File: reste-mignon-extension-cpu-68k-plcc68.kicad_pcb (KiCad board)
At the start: 4 copper layers, 99.1 x 99.1 mm, 20 parts, among them J1 RESTE_MIGNON_CPU_CONNECTOR_A, J2 RESTE_MIGNON_CPU_CONNECTOR_B, U1 MC68000_PLCC_68_PHY

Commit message: switch RN5 and RN6 to ease routing
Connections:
- RN5 pad 2: /D0 -> /D8
- RN5 pad 3: /D1 -> /D9
- RN5 pad 4: /D2 -> /D10
- RN5 pad 5: /D3 -> /D11
- RN5 pad 6: /D4 -> /D12
- RN5 pad 7: /D5 -> /D13
- RN5 pad 8: /D6 -> /D14
- RN5 pad 9: /D7 -> /D15
- RN6 pad 2: /D8 -> /D0
- RN6 pad 3: /D9 -> /D1
- RN6 pad 4: /D10 -> /D2
- RN6 pad 5: /D11 -> /D3
- RN6 pad 6: /D12 -> /D4
- RN6 pad 7: /D13 -> /D5
- RN6 pad 8: /D14 -> /D6
- RN6 pad 9: /D15 -> /D7
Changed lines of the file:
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@@
       (net 1 "/VCC") (pinfunction "common") (pintype "passive"))
     (pad "2" thru_hole oval (at 2.54 0 90) (size 1.6 1.6) (drill 0.8) (layers "*.Cu" "*.Mask")
-      (net 42 "/D0") (pinfunction "R1") (pintype "passive"))
+      (net 50 "/D8") (pinfunction "R1") (pintype "passive"))
     (pad "3" thru_hole oval (at 5.08 0 90) (size 1.6 1.6) (drill 0.8) (layers "*.Cu" "*.Mask")
-      (net 41 "/D1") (pinfunction "R2") (pintype "passive"))
+      (net 49 "/D9") (pinfunction "R2") (pintype "passive"))
     (pad "4" thru_hole oval (at 7.62 0 90) (size 1.6 1.6) (drill 0.8) (layers "*.Cu" "*.Mask")
-      (net 43 "/D2") (pinfunction "R3") (pintype "passive"))
+      (net 52 "/D10") (pinfunction "R3") (pintype "passive"))
     (pad "5" thru_hole oval (at 10.16 0 90) (size 1.6 1.6) (drill 0.8) (layers "*.Cu" "*.Mask")
-      (net 45 "/D3") (pinfunction "R4") (pintype "passive"))
+      (net 51 "/D11") (pinfunction "R4") (pintype "passive"))
     (pad "6" thru_hole oval (at 12.7 0 90) (size 1.6 1.6) (drill 0.8) (layers "*.Cu" "*.Mask")
-      (net 44 "/D4") (pinfunction "R5") (pintype "passive"))
+      (net 53 "/D12") (pinfunction "R5") (pintype "passive"))
     (pad "7" thru_hole oval (at 15.24 0 90) (size 1.6 1.6) (drill 0.8) (layers "*.Cu" "*.Mask")
-      (net 47 "/D5") (pinfunction "R6") (pintype "passive"))
+      (net 55 "/D13") (pinfunction "R6") (pintype "passive"))
     (pad "8" thru_hole oval (at 17.78 0 90) (size 1.6 1.6) (drill 0.8) (layers "*.Cu" "*.Mask")
-      (net 46 "/D6") (pinfunction "R7") (pintype "passive"))
+      (net 54 "/D14") (pinfunction "R7") (pintype "passive"))
     (pad "9" thru_hole oval (at 20.32 0 90) (size 1.6 1.6) (drill 0.8) (layers "*.Cu" "*.Mask")
-      (net 48 "/D7") (pinfunction "R8") (pintype "passive"))
+      (net 57 "/D15") (pinfunction "R8") (pintype "passive"))
     (model "${KICAD6_3DMODEL_DIR}/Resistor_THT.3dshapes/R_Array_SIP9.wrl"
       (offset (xyz 0 0 0))
@@
       (net 1 "/VCC") (pinfunction "common") (pintype "passive"))
     (pad "2" thru_hole oval (at 2.54 0 90) (size 1.6 1.6) (drill 0.8) (layers "*.Cu" "*.Mask")
-      (net 50 "/D8") (pinfunction "R1") (pintype "passive"))
+      (net 42 "/D0") (pinfunction "R1") (pintype "passive"))
     (pad "3" thru_hole oval (at 5.08 0 90) (size 1.6 1.6) (drill 0.8) (layers "*.Cu" "*.Mask")
-      (net 49 "/D9") (pinfunction "R2") (pintype "passive"))
+      (net 41 "/D1") (pinfunction "R2") (pintype "passive"))
     (pad "4" thru_hole oval (at 7.62 0 90) (size 1.6 1.6) (drill 0.8) (layers "*.Cu" "*.Mask")
-      (net 52 "/D10") (pinfunction "R3") (pintype "passive"))
+      (net 43 "/D2") (pinfunction "R3") (pintype "passive"))
     (pad "5" thru_hole oval (at 10.16 0 90) (size 1.6 1.6) (drill 0.8) (layers "*.Cu" "*.Mask")
-      (net 51 "/D11") (pinfunction "R4") (pintype "passive"))
+      (net 45 "/D3") (pinfunction "R4") (pintype "passive"))
     (pad "6" thru_hole oval (at 12.7 0 90) (size 1.6 1.6) (drill 0.8) (layers "*.Cu" "*.Mask")
-      (net 53 "/D12") (pinfunction "R5") (pintype "passive"))
+      (net 44 "/D4") (pinfunction "R5") (pintype "passive"))
     (pad "7" thru_hole oval (at 15.24 0 90) (size 1.6 1.6) (drill 0.8) (layers "*.Cu" "*.Mask")
-      (net 55 "/D13") (pinfunction "R6") (pintype "passive"))
+      (net 47 "/D5") (pinfunction "R6") (pintype "passive"))
     (pad "8" thru_hole oval (at 17.78 0 90) (size 1.6 1.6) (drill 0.8) (layers "*.Cu" "*.Mask")
-      (net 54 "/D14") (pinfunction "R7") (pintype "passive"))
+      (net 46 "/D6") (pinfunction "R7") (pintype "passive"))
     (pad "9" thru_hole oval (at 20.32 0 90) (size 1.6 1.6) (drill 0.8) (layers "*.Cu" "*.Mask")
-      (net 57 "/D15") (pinfunction "R8") (pintype "passive"))
+      (net 48 "/D7") (pinfunction "R8") (pintype "passive"))
     (model "${KICAD6_3DMODEL_DIR}/Resistor_THT.3dshapes/R_Array_SIP9.wrl"
       (offset (xyz 0 0 0))

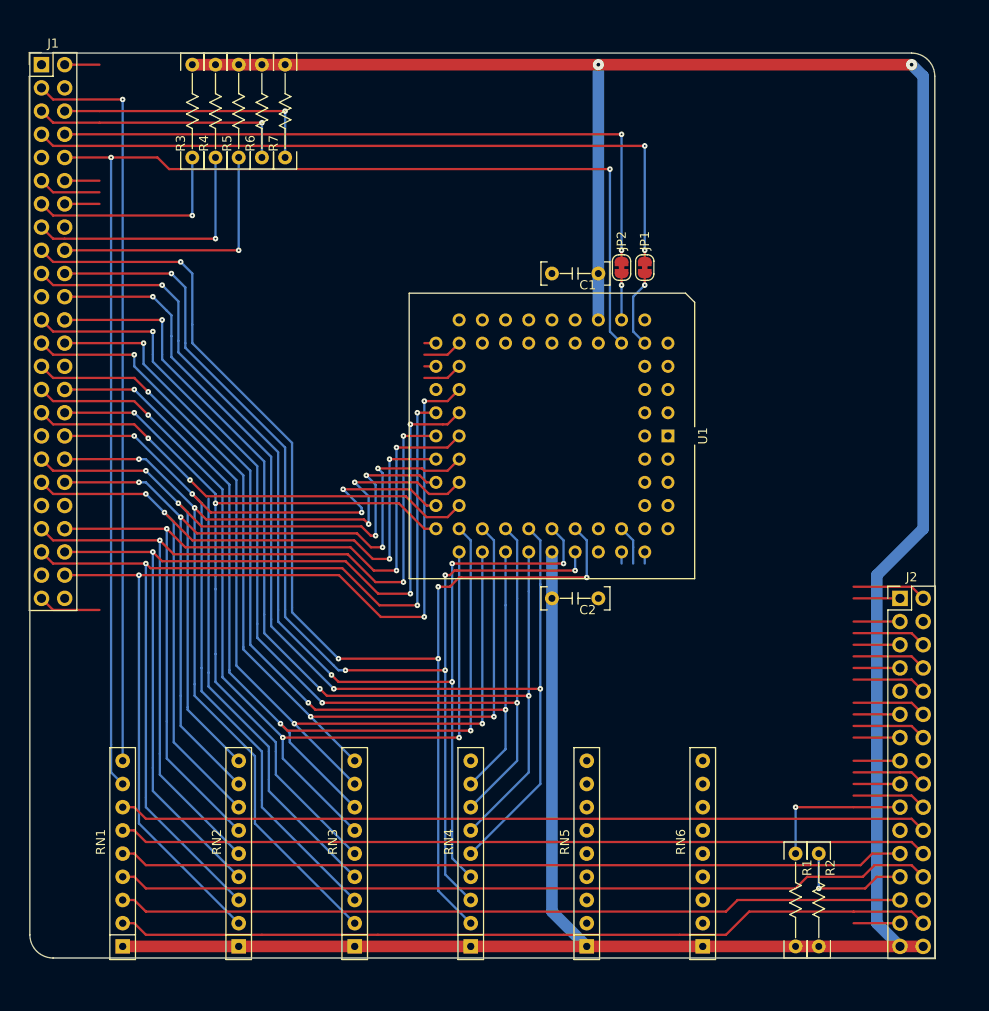
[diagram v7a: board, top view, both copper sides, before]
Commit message: pcb session -- adjust constraints to pass drc, silkscreen -- start using free angles
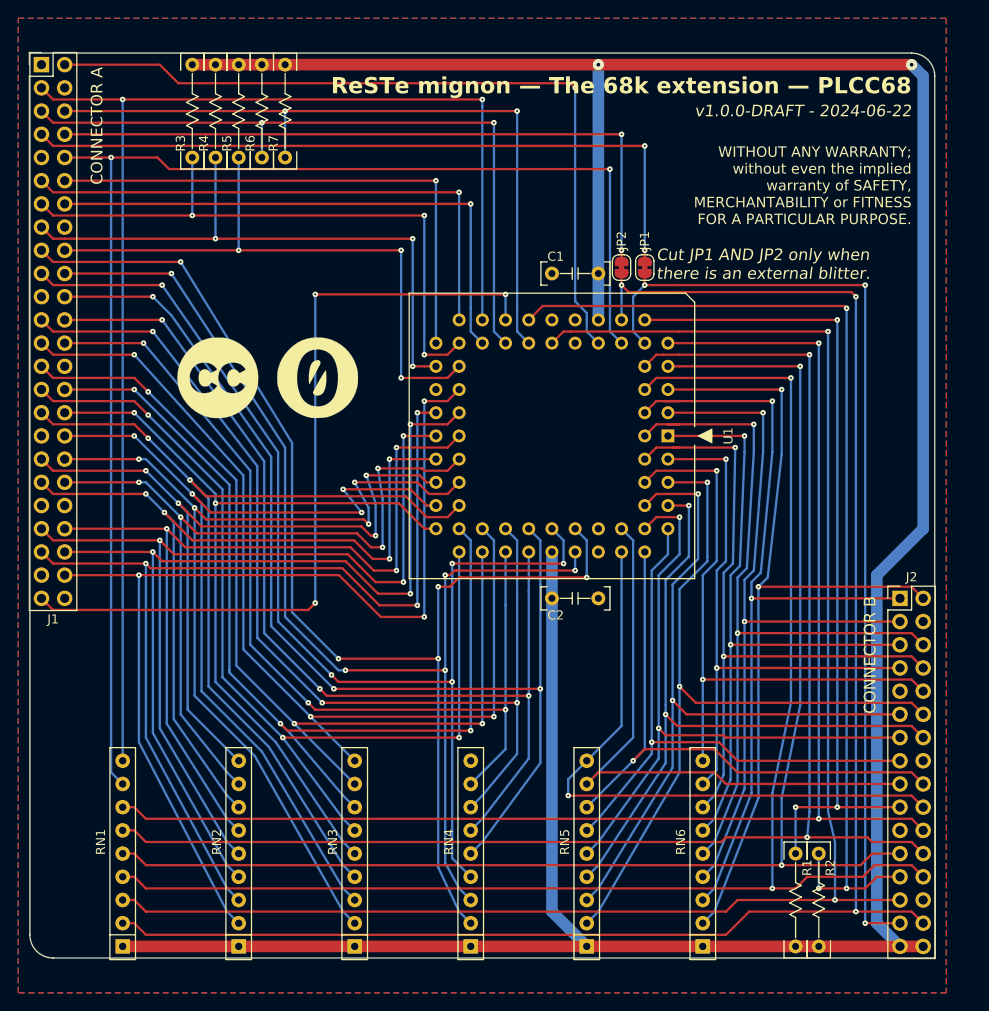
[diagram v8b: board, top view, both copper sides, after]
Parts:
- added G***: LOGO, cliparts:logo--cc--cc, F.Cu at (73.9, 137.2)
- added G***: LOGO, cliparts:logo--cc--zero, F.Cu at (84.8, 137.2)
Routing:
- net /~{RESET}: track 13.2 -> 112.3 mm, vias 1 -> 3
- net /~{BGACK}: track 94.8 -> 188.3 mm, vias 1 -> 3
- net /~{HALT}: track 86.1 -> 179.2 mm, vias 0 -> 2
- net /~{BG}: track 13.8 -> 106.5 mm, vias 1 -> 3
- net /D1: track 5.08 -> 88.7 mm, vias 0 -> 2
- net /D0: track 8.15 -> 91.4 mm, vias 0 -> 2
- net /CLK: track 3.81 -> 85.9 mm, vias 0 -> 1
- net /E: track 6.88 -> 88.2 mm, vias 0 -> 3
- net /D8: track 8.15 -> 84.7 mm, vias 0 -> 2
- net /D9: track 5.08 -> 80.3 mm, vias 0 -> 2
- net /D3: track 8.15 -> 83.0 mm, vias 0 -> 2
- net /D2: track 5.08 -> 79.8 mm, vias 0 -> 2
- net /~{DTACK}: track 16.5 -> 90.9 mm, vias 1 -> 3
- net /~{AS}: track 89.7 -> 162.3 mm, vias 0 -> 2
- net /~{LDS}: track 88.7 -> 160.5 mm, vias 0 -> 2
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- added copper zone on B.Cu, net (none)
- added copper zone on F.Cu, net (none)
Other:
- board text added: "${REVISION} - ${ISSUE_DATE}"
- board text added: "${TITLE}"
- board text added: "CONNECTOR A"
- board text added: "CONNECTOR B"
- board text added: "Cut JP1 AND JP2 only when there is an external blitter."
- board text added: "WITHOUT ANY WARRANTY; without even the implied warranty of SAFETY, MERCHANTABILITY or FITNESS FOR A PARTICULAR PURPOSE."
